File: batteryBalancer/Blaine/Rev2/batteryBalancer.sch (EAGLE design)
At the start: 50 parts

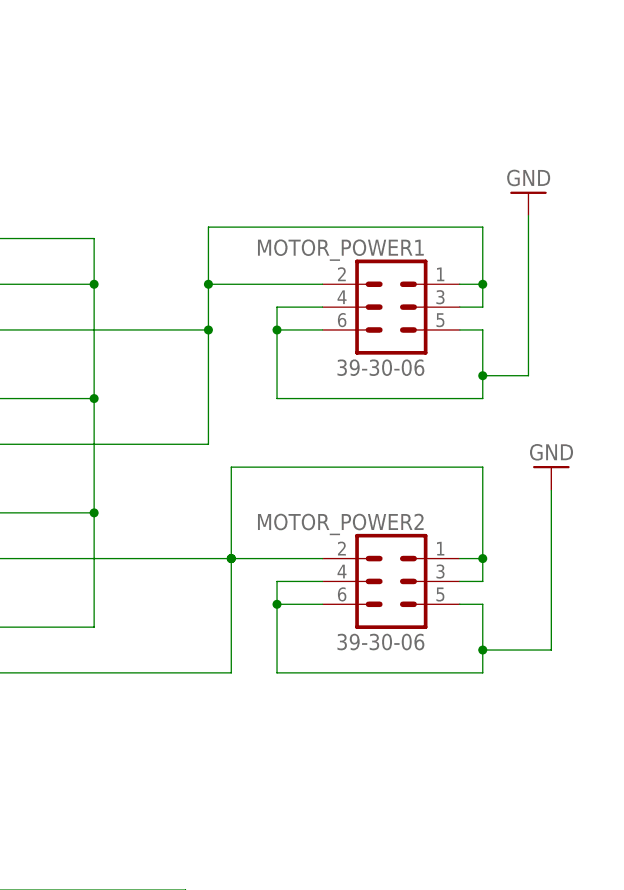
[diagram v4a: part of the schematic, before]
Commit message: Added 8 pin connector
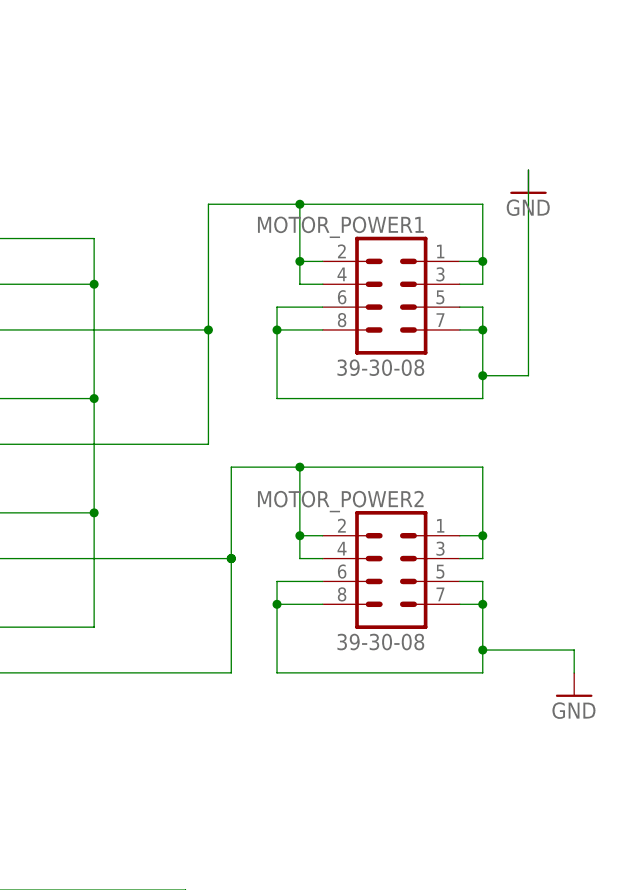
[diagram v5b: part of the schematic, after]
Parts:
- MOTOR_POWER1, MOTOR_POWER2: value 39-30-06 -> 39-30-08; device con-molex-mini-fit:39-30-06 -> con-molex-mini-fit:39-30-08
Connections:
- net GND: now also MOTOR_POWER1.7, MOTOR_POWER1.8, MOTOR_POWER2.7, MOTOR_POWER2.8; no longer MOTOR_POWER1.4, MOTOR_POWER2.4
- net MOTOR_POWER1: now also MOTOR_POWER1.4
- net MOTOR_POWER2: now also MOTOR_POWER2.4
